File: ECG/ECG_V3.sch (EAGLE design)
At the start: 32 parts, among them U1 AD8232, U3 BGM111-VISUAL-A

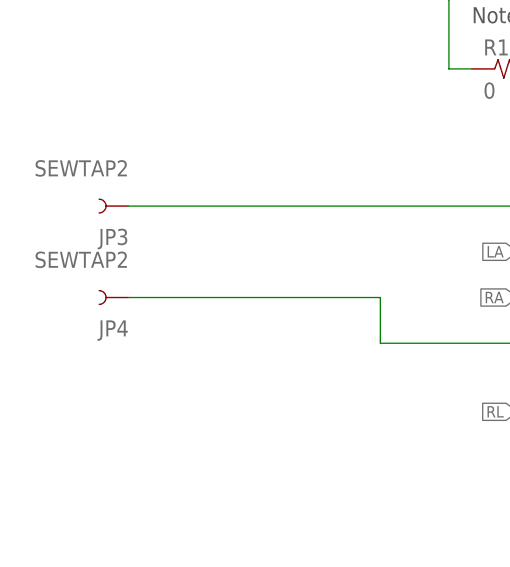
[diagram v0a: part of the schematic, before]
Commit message: Modified Sewtap pads and reduced board size
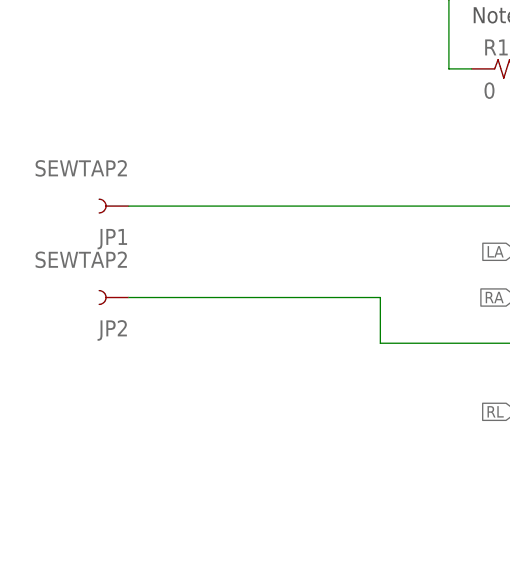
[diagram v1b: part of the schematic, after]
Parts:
- renumbered JP3 to JP1, JP4 to JP2
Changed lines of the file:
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@@
 <part name="J2" library="tag-connect" deviceset="TC2030" device="-MCP-NL"/>
 <part name="SUPPLY14" library="SparkFun-Aesthetics" deviceset="3.3V" device=""/>
-<part name="JP3" library="LilyPad-Wearables" deviceset="SEWTAP" device="2"/>
-<part name="JP4" library="LilyPad-Wearables" deviceset="SEWTAP" device="2"/>
+<part name="JP1" library="LilyPad-Wearables" deviceset="SEWTAP" device="2"/>
+<part name="JP2" library="LilyPad-Wearables" deviceset="SEWTAP" device="2"/>
 </parts>
 <sheets>
@@
 <instance part="J2" gate="G$1" x="157.48" y="-17.78" rot="R180"/>
 <instance part="SUPPLY14" gate="G$1" x="180.34" y="-22.86" rot="R270"/>
-<instance part="JP3" gate="G$1" x="27.94" y="134.62" rot="R180"/>
-<instance part="JP4" gate="G$1" x="27.94" y="124.46" rot="R180"/>
+<instance part="JP1" gate="G$1" x="27.94" y="134.62" rot="R180"/>
+<instance part="JP2" gate="G$1" x="27.94" y="124.46" rot="R180"/>
 </instances>
 <busses>
@@
 <junction x="81.28" y="129.54"/>
 <label x="73.66" y="129.54" size="1.27" layer="95" rot="R180" xref="yes"/>
-<pinref part="JP3" gate="G$1" pin="1"/>
 <wire x1="30.48" y1="134.62" x2="76.2" y2="134.62" width="0.1524" layer="91"/>
 <wire x1="76.2" y1="134.62" x2="76.2" y2="129.54" width="0.1524" layer="91"/>
 <junction x="76.2" y="129.54"/>
+<pinref part="JP1" gate="G$1" pin="1"/>
 </segment>
 </net>
@@
 <junction x="88.9" y="124.46"/>
 <label x="73.66" y="124.46" size="1.27" layer="95" rot="R180" xref="yes"/>
-<pinref part="JP4" gate="G$1" pin="1"/>
 <wire x1="30.48" y1="124.46" x2="58.42" y2="124.46" width="0.1524" layer="91"/>
 <wire x1="58.42" y1="124.46" x2="58.42" y2="119.38" width="0.1524" layer="91"/>
@@
 <wire x1="81.28" y1="119.38" x2="81.28" y2="124.46" width="0.1524" layer="91"/>
 <junction x="81.28" y="124.46"/>
-</segment>
-</net>
+<pinref part="JP2" gate="G$1" pin="1"/>
+</segment>
+</net>
